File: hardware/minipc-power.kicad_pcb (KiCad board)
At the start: 4 copper layers, 52 x 36 mm, 104 parts, among them J1 USB-C HRO TYPE-C-31-M-12, J10 VSYS (switch), J11 CHG, J12 PG_CHG, J13 VBAT_SENSE, J14 3V3_PG, J15 GND, J16 GND, J17 GND, J2 BAT+, J3 BAT-, J4 NTC, J5 NTC-, J6 +12V OUT, J7 +5V OUT, J8 +3V3 OUT, J9 EN (switch), Q1 CSD13202Q2, Q2 CSD13202Q2, Q3 CSD13202Q2, Q4 CSD25404Q3, Q5 CSD25404Q3, Q6 2N7002, U1 CH224Q, U2 BQ25606, U3 HY2113-MB1A, U4 TPS61178, U5 TPS61088-Q1, U6 TPS63802

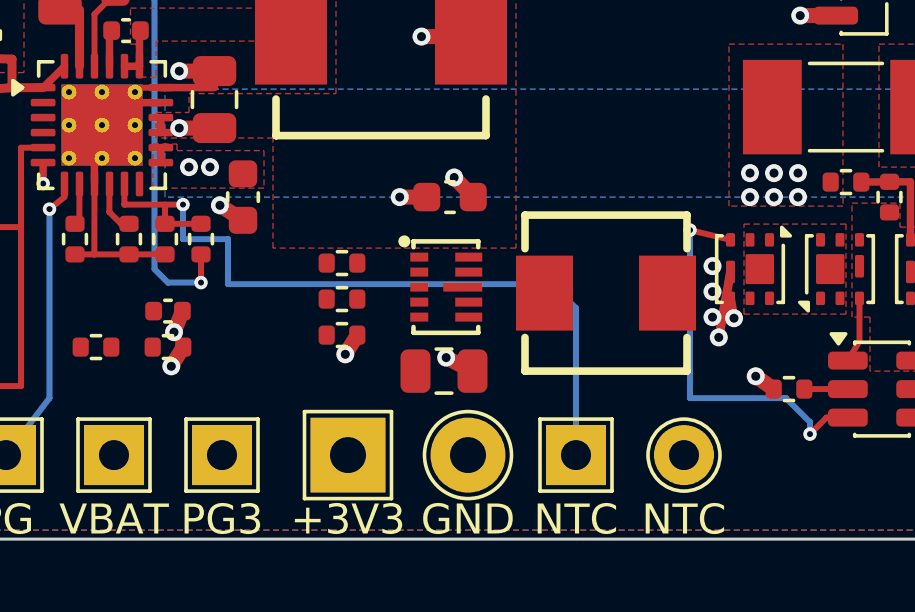
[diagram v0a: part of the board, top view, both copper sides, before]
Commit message: Route 3.3V buck-boost per TPS63802 fig. 12-1 / WEBENCH d36; TS rerouted off U6
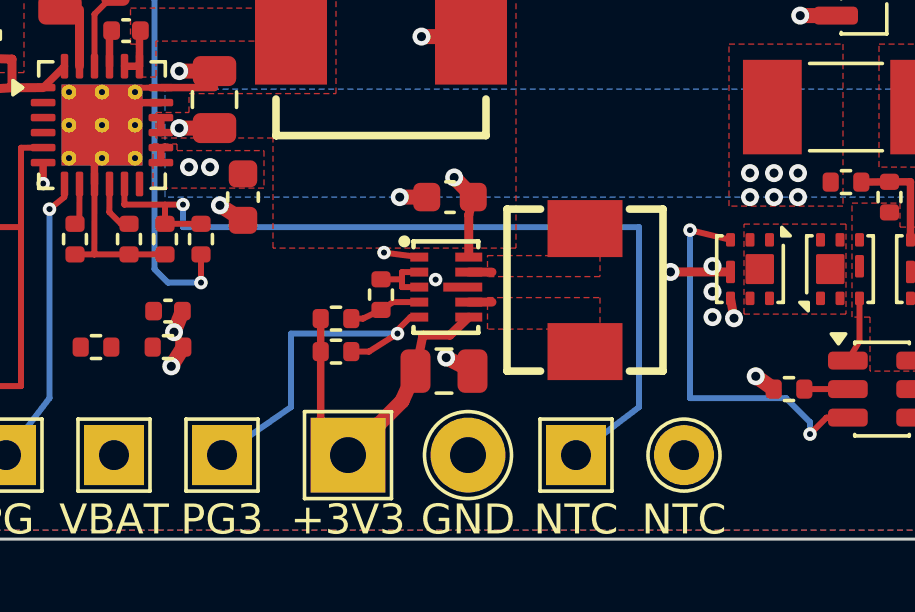
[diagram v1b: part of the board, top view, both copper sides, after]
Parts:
- moved R26 2.96 mm to (126.4, 129.8), turned to 180 degrees
- moved R25 1.87 mm to (127.9, 127.8), turned to 90 degrees
- moved L4 0.71 mm to (134.7, 127.7), turned to -90 degrees
- moved R24 0.68 mm to (126.4, 128.7)
- turned C33 to 180 degrees
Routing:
- net /3V3_PG: track 0.00 -> 11.5 mm, vias 0 -> 1
- net +3V3: track 0.00 -> 10.3 mm
- net Net-(U2-TS): track 25.5 -> 29.1 mm
- net Net-(U6-FB): track 0.00 -> 2.41 mm
- net VSYS: track 23.5 -> 25.4 mm
- net GND: track 65.8 -> 67.1 mm
- net /EN: track 4.85 -> 6.03 mm, vias 3 -> 4
- net Net-(U6-L2): track 0.00 -> 0.78 mm
- net Net-(U6-L1): track 0.00 -> 0.78 mm
- added copper zone on F.Cu, net Net-(U6-L1)
- added copper zone on F.Cu, net Net-(U6-L2)

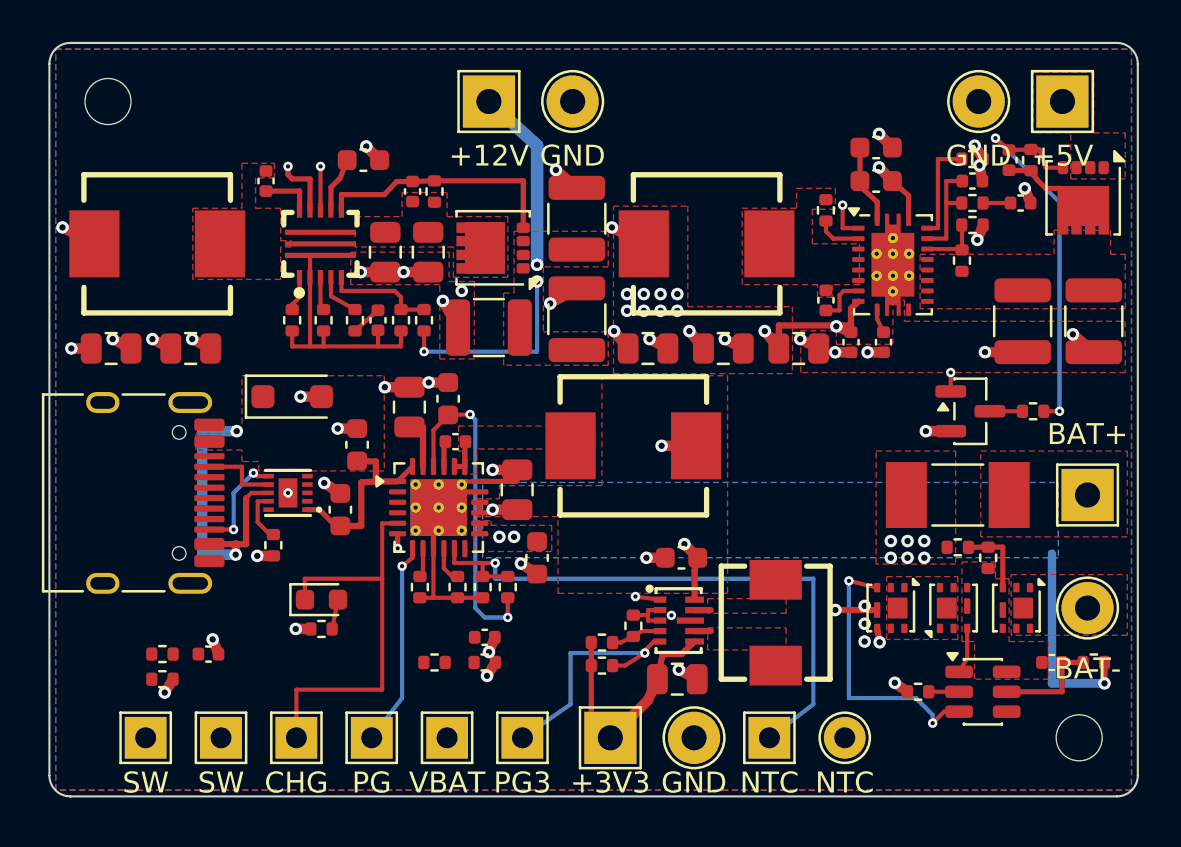
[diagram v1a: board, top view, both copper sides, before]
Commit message: Route EN bus, switch pad, VBAT sense; board fully routed (DRC 0, unconnected 0)
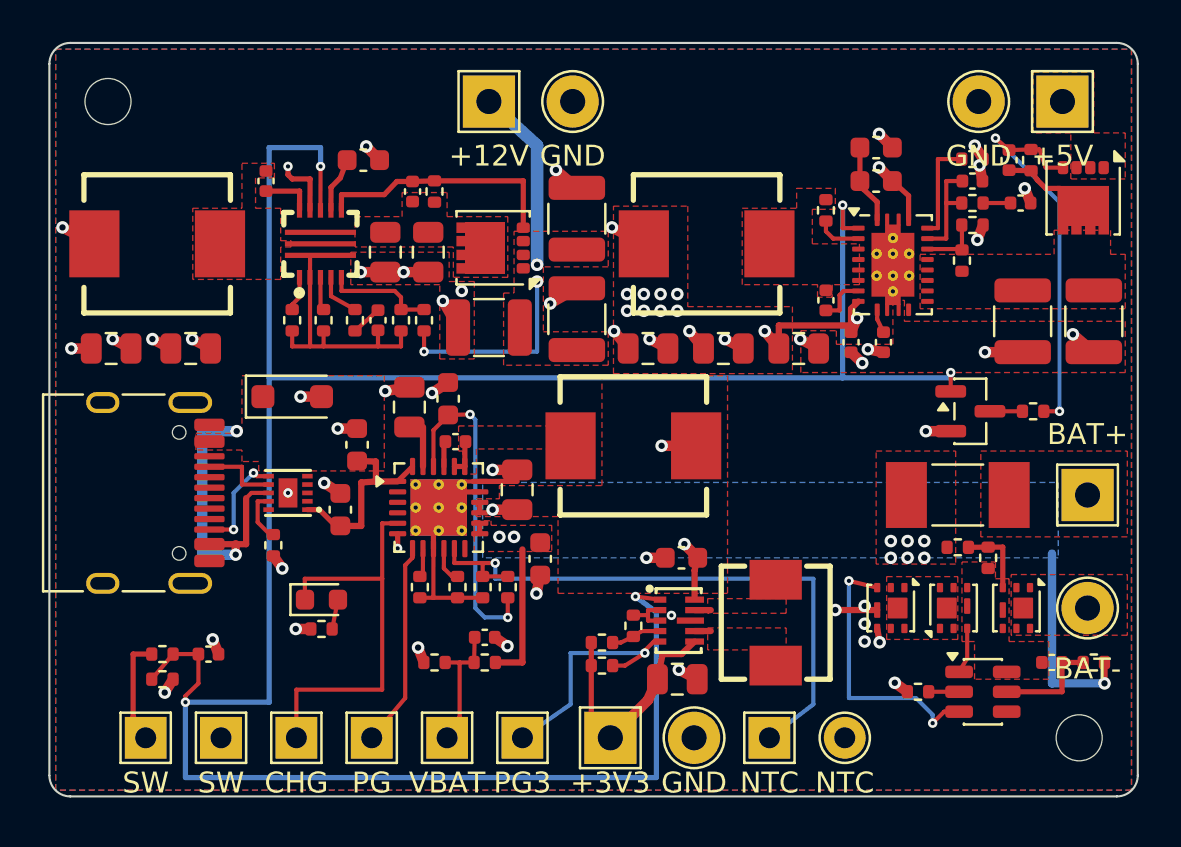
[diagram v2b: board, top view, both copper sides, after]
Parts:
- moved R29 2.40 mm to (120.8, 129.6), turned to 180 degrees
- moved R30 2.40 mm to (118.4, 129.6), turned to 180 degrees
- moved C6 0.16 mm to (123.5, 124.7)
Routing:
- net /EN: track 6.03 -> 121.5 mm, vias 4 -> 5
- net BAT: track 10.2 -> 16.9 mm
- net Net-(C36-Pad1): track 0.00 -> 6.35 mm
- net Net-(J9-Pad1): track 0.00 -> 5.06 mm
- net /PG_CHG: vias 1 -> 0

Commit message: Regenerate board with C37 and pad-label fixes; DRC summary no longer hides silk warnings
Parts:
- added C37: 1uF, Capacitor_SMD:C_0402_1005Metric, F.Cu at (112.2, 104.9)
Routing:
- net VSYS: track 25.4 -> 27.2 mm, vias 21 -> 22
- net GND: track 67.1 -> 67.8 mm, vias 46 -> 47

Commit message: Design review 2026-10-24 (kicad-skills board review): fixes, datasheet links on every part
Fixes found by the review (docs/review-2026-10-24.md):
- R25 91k: LCSC C4147 (2 in stock) -> C144733
- U5 TPS61088-Q1: C38 1 uF 0402 at the VOUT pins (datasheet fig. 13 C9, fig. 21); NC pins 11/12 tied to GND
  as the pin table asks (symbol pins passive)
- Q5 load switch: C32 10 nF -> 100 nF (~1 ms turn-on; inrush could trip the BQ25606 BATFET OCP latch)
- U6 TPS63802: C33 ground on a top-layer track to PGND pin 8 (fig. 12-1); C_OUT side still open
- R7 330 -> 100 R (HY2113 100-200 R); R16 178k -> 100k (Q4 Vgs margin to +/-12 V)
- power-design.md / layout-compliance.md corrected against the board (R_ICHG, L4, SS, COUT1, Q2/Q3 common drain)

Datasheet links: every BOM part carries one in the schematic and on the board (TI symlinks for TI parts, else the
LCSC page of the exact part). The redrawn symbols had dropped JLCImport's links, passives kept KiCad's "~" and
board_setup never copied the netlist's datasheet; schgen, symbols.library() and board_setup now refuse a BOM part
without one. kicad-skills partfields.py --online: 0 problems (176 before).

Pin decisions for U2.2 and U3.4 (NC per their pin tables), required by kicad-skills' stricter nc_audit.
KiCad's own project / fab-toolkit files and the production outputs (gerbers, BOM, positions) included.
skill-gaps.md: gaps 34-45 from running the review skills.
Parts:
- added C38: 1uF, Capacitor_SMD:C_0402_1005Metric, F.Cu at (143.2, 113.0)
- C32: value 10nF -> 100nF
- R16: value 178k -> 100k
- R7: value 330 -> 100
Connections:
- U5 pad 11: unconnected-(U5-NC-Pad11) -> GND
- U5 pad 12: unconnected-(U5-NC-Pad12) -> GND
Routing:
- net GND: track 67.8 -> 73.7 mm, vias 47 -> 48

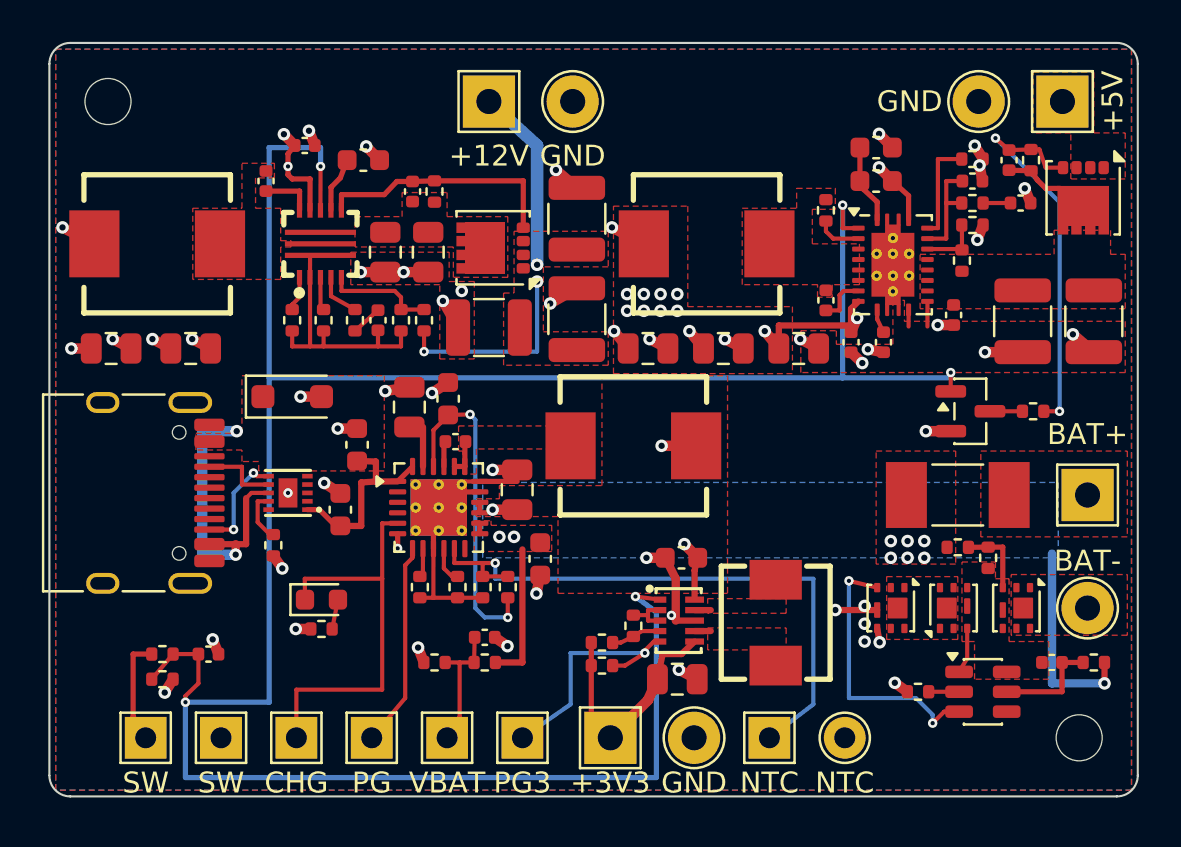
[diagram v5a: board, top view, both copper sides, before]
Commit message: Heat: thermal budget, GND stitching vias, B.Cu copper under the protection FETs
docs/thermal.md: heat sources per operating case (battery path dominates at high load: 5.0 W on the board at 15 W
from an empty cell), board temperature in a closed box (15 W is a peak rating, ~10-12 W continuous), hot spots,
options. route_plan: stitch_grid() edge ring + interior GND vias (edge vias 6 -> 34, worst edge gap 57 -> 17 mm),
second vias at C18/C1, same-net B.Cu islands with 16 vias under Q1-Q3 (R7 BAT feed moved to the right edge).
DRC 0 violations, 0 unconnected, parity 0. hardware/production/ predates these vias: regenerate before ordering.
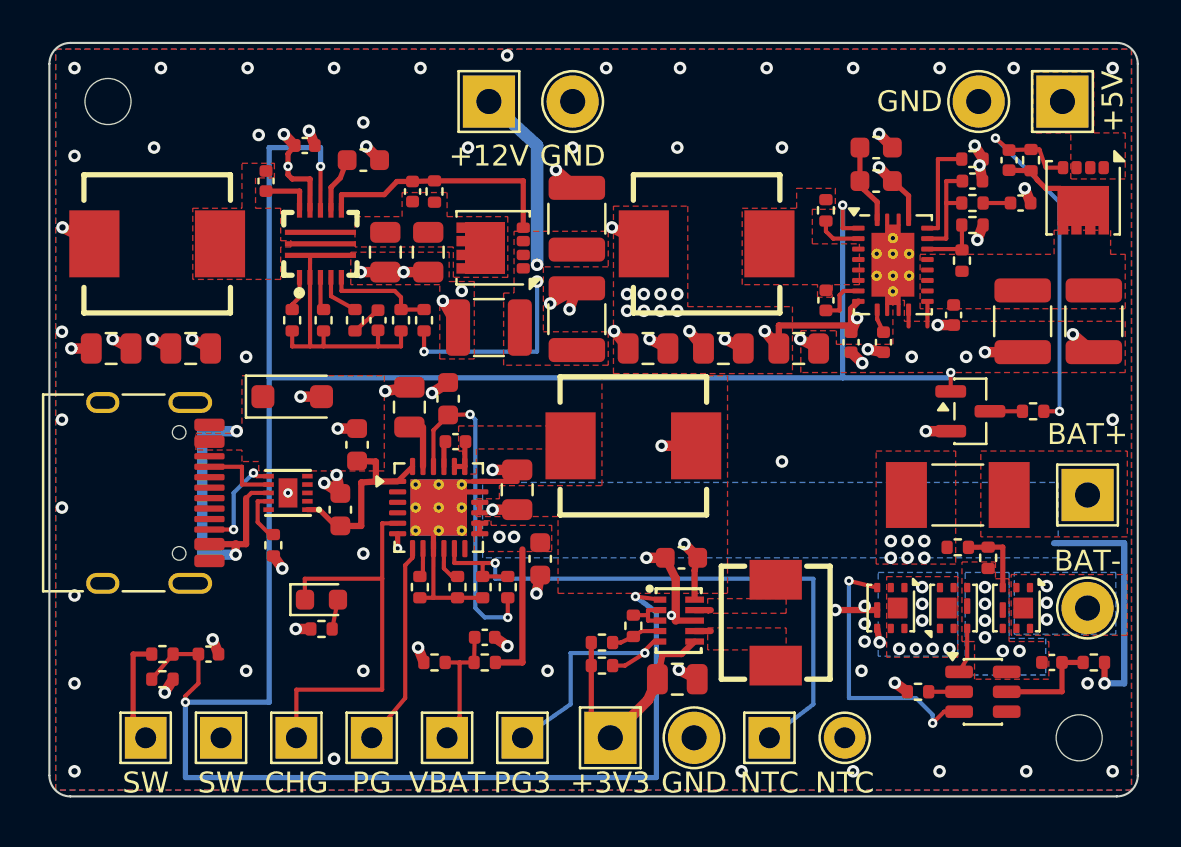
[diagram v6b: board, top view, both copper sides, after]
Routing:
- net BAT: track 16.9 -> 19.2 mm
- net GND: track 73.7 -> 75.7 mm, vias 48 -> 94
- net Net-(U3-VSS): vias 0 -> 6
- net Net-(Q2-D-Pad1): vias 0 -> 7
- net Net-(J3-Pad1): vias 0 -> 3
- added copper zone on B.Cu, net Net-(J3-Pad1)
- added copper zone on B.Cu, net Net-(Q2-D-Pad1)
- added copper zone on B.Cu, net Net-(U3-VSS)

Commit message: Protection FETs: DMN1004UFV, block re-laid out with B.Cu copper; heat 5.0 -> 3.4 W at 15 W
Q1-Q3 CSD13202Q2 (8.4 mOhm at 3 V) -> Diodes DMN1004UFV (C316138, 3.2 / 5.1 mOhm at 2.5 V, PowerDI3333-8;
KiCad Diodes_PowerDI3333-8 checked against the datasheet's suggested pads; JLCImport 3D model, orientation checked
by the pin-1 dot). FET loss at 15 W from an empty cell 1.72 -> 0.53 W, board 5.0 -> 3.4 W (docs/thermal.md).
The 3.3 mm parts no longer fit in a row: Q2 | Q1 face across the CELLN gap, Q1's drain at J3, Q3 under Q2's drain;
U3 between Q3 and H2's keep-out, R7-R10 / C8 under J3. Same-net B.Cu islands joined by vias; OD, CS and Q1's gate
take short B.Cu lanes. U3 stays HY2113-MB1A: its FET-sensed trip moves to ~18-46 A (power-design s3).
A Vishay SiSS80DN was chosen first and dropped: stocked on LCSC China only, not for JLCPCB global assembly.

routing.via_near: no via on any pad but the one it stitches (two had landed in Q3's neighbouring source pads).
docs/review_config.json: the review's power runs, updated for the new pins and net names.
skill-gaps.md 46-52. DRC 0, ERC 0, unconnected 0, parity 0, board_lint 0, pin decisions and part fields clean;
bom_check (global) 0 problems. hardware/production/ still predates this board.
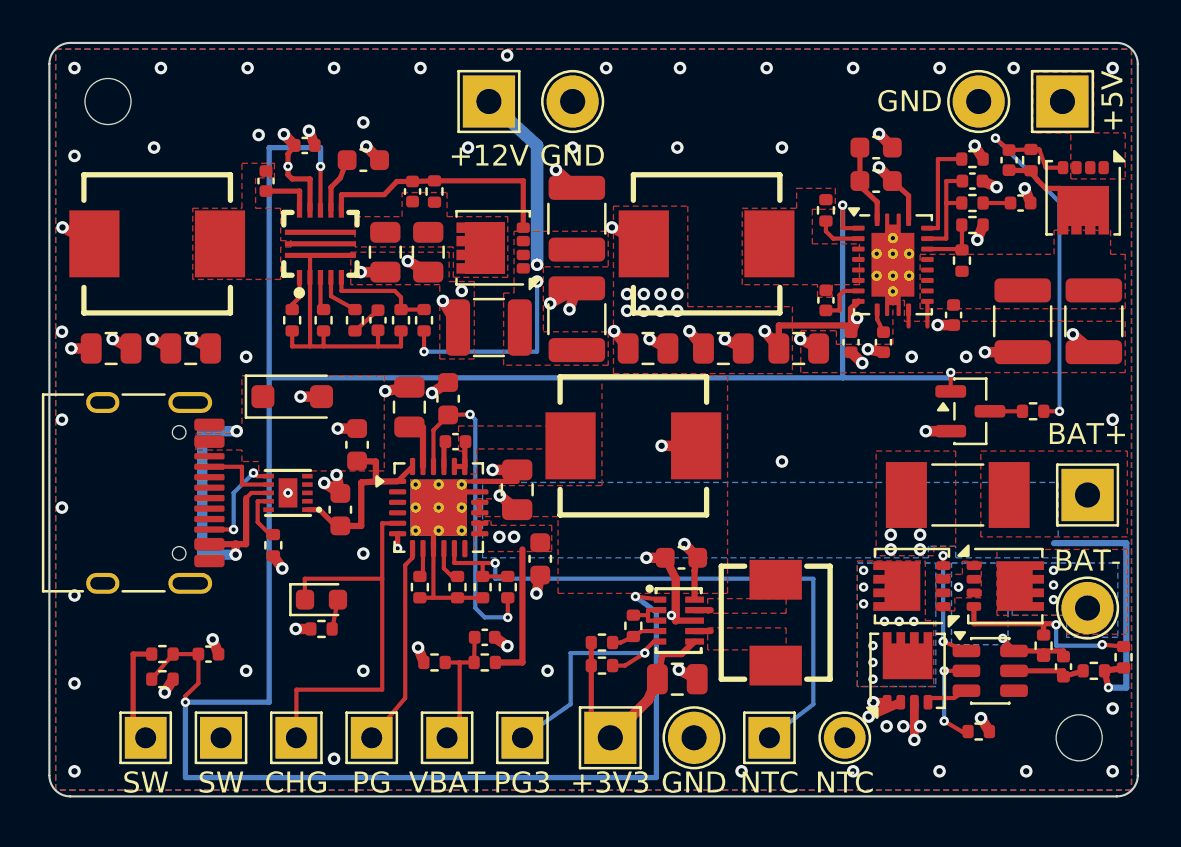
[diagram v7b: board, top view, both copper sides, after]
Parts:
- Q1, Q2, Q3: value CSD13202Q2 -> DMN1004UFV; footprint Package_SON:Texas_DQK -> Package_SON:Diodes_PowerDI3333-8
- moved R9 9.50 mm to (151.3, 129.3), turned to 90 degrees
- moved R10 4.97 mm to (147.5, 128.8)
- moved R8 3.47 mm to (144.4, 132.9), turned to 0 degrees
- moved Q3 3.10 mm to (141.0, 130.0), turned to 90 degrees
- moved Q2 2.25 mm to (141.2, 126.0), turned to 180 degrees
- moved Q1 1.18 mm to (145.7, 126.0), turned to 0 degrees
- moved U3 1.06 mm to (144.9, 130.0)
- moved C8 0.59 mm to (148.4, 129.8), turned to 90 degrees
- moved R7 0.40 mm to (149.9, 130.0)
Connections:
- J3 pad 1: Net-(J3-Pad1) -> Net-(Q1-D)
- Q1 pad 1: Net-(J3-Pad1) -> Net-(U3-VSS)
- Q1 pad 2: Net-(J3-Pad1) -> Net-(U3-VSS)
- Q1 pad 3: Net-(Q1-G) -> Net-(U3-VSS)
- Q1 pad 4: Net-(U3-VSS) -> Net-(Q1-G)
- Q1 pad 5: Net-(J3-Pad1) -> Net-(Q1-D)
- Q2 pad 1: Net-(Q2-D-Pad1) -> Net-(U3-VSS)
- Q2 pad 2: Net-(Q2-D-Pad1) -> Net-(U3-VSS)
- Q2 pad 3: Net-(Q2-G) -> Net-(U3-VSS)
- Q2 pad 4: Net-(U3-VSS) -> Net-(Q2-G)
- Q2 pad 5: Net-(Q2-D-Pad1) -> Net-(Q2-D)
- Q3 pad 1: Net-(Q2-D-Pad1) -> GND
- Q3 pad 2: Net-(Q2-D-Pad1) -> GND
- Q3 pad 3: Net-(Q3-G) -> GND
- Q3 pad 4: GND -> Net-(Q3-G)
- Q3 pad 5: Net-(Q2-D-Pad1) -> Net-(Q2-D)
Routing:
- net Net-(Q3-G): track 13.2 -> 2.13 mm, vias 2 -> 0
- net Net-(Q1-G): track 3.58 -> 9.52 mm, vias 0 -> 2
- net Net-(U3-VSS): track 0.00 -> 3.70 mm, vias 6 -> 2
- net Net-(Q2-G): track 2.18 -> 5.78 mm, vias 0 -> 2
- net Net-(U3-CS): track 1.45 -> 4.74 mm, vias 0 -> 2
- net Net-(U3-VDD): track 5.05 -> 3.62 mm
- net GND: track 75.7 -> 77.1 mm
- net BAT: track 19.2 -> 20.1 mm, vias 9 -> 7
- net Net-(Q2-D-Pad1): vias 7 -> 0
- net Net-(Q2-D): vias 0 -> 9
- net Net-(Q1-D): vias 0 -> 3
- net Net-(J3-Pad1): vias 3 -> 0
- added copper zone on B.Cu, net Net-(Q1-D)
- added copper zone on F.Cu, net Net-(Q1-D)
- added copper zone on B.Cu, net Net-(Q2-D)
- added copper zone on F.Cu, net Net-(Q2-D)
- removed copper zone on B.Cu, net Net-(J3-Pad1)
- removed copper zone on F.Cu, net Net-(J3-Pad1)
- removed copper zone on B.Cu, net Net-(Q2-D-Pad1)
- removed copper zone on F.Cu, net Net-(Q2-D-Pad1)
